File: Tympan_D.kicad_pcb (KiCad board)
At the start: 4 copper layers, 38 x 74 mm, 116 parts, among them IC1 MK66FX1M0VMD18, IC2 MKL02Z32VFG4, IC3 BC127, J1 SJ-3523-SMT-TR, J2 SJ-3524-SMT-TR-PI, J3 alt Power Pads, P1 USB_OTG, P10 CONN_01X01, P2 CONN_01X06, P3 CONN_01X06, P4 CONN_01X06, P5 CONN_01X06, P6 CONN_01X03, P7 CONN_01X01, P8 CONN_01X01, P9 CONN_01X01, SW1 CL-SB-22A, SW2 TACT_SWITCH, U1 AP2210K-3.3TRG1, U2 TLV320AIC3206IRSBT, U3 74LVC1G66, U4 LP5907MFX-1.8, U5 MCP73831, Y1 32.768kHz, Y2 16MHz

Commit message: Made Production Files
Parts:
- moved G*** 3.59 mm to (133.8, 80.5)
- moved G*** 2.10 mm to (133.8, 65.1)
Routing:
- net /IN2_R: track 28.2 -> 27.5 mm
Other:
- board text added: "1V8|M_BIAS_1 IN1_R|MCLK IN1_L|BCLK LOL|WCLK LOR|RST_1 GND|GND"
- board text added: "Alt Power 12V Max Cut V_BUS"
- board text added: "Designed in Brooklyn, NY USA Made in Taipei, Taiwan"
- board text added: "GND +V"
- board text added: "PDM_DAT|3V3 PDM_CLK|DOUT MISO_2|DIN MOSI_2|SDA2 SCK_2|SCL2 SS_2|GND"
- board text removed: "1V8/M_BIAS_1 IN1_R/MCLK IN1_L/BCLK LOL/WCLK LOR/RST_1 GND/GND"
- board text removed: "Alt Power 12V Max"
- board text removed: "Designed in Brooklyn, NY"
- board text removed: "GND BATT"
- board text removed: "TX_3/3V3 RX_3/DOUT MISO_2/DIN MOSI_2/SDA2 SCK_2/SCL2 SS_2/GND"
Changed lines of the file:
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@@
     (thickness 1.6)
     (drawings 77)
-    (tracks 1333)
+    (tracks 1335)
     (zones 0)
     (modules 116)
@@
     (36 B.SilkS user)
     (37 F.SilkS user)
-    (38 B.Mask user hide)
-    (39 F.Mask user hide)
+    (38 B.Mask user)
+    (39 F.Mask user)
     (40 Dwgs.User user hide)
     (41 Cmts.User user hide)
     (42 Eco1.User user hide)
-    (43 Eco2.User user)
+    (43 Eco2.User user hide)
     (44 Edge.Cuts user)
     (45 Margin user)
@@
   )
   (setup
-    (last_trace_width 0.2032)
+    (last_trace_width 0.25)
     (user_trace_width 0.1778)
     (user_trace_width 0.2032)
@@
     (descr BGA-144-1mm)
     (attr smd)
-    (fp_text reference IC1 (at -5.226 7.6866 180) (layer B.SilkS)
+    (fp_text reference IC1 (at -7.876 6.0866 180) (layer B.SilkS)
       (effects (font (size 1 1) (thickness 0.15)) (justify mirror))
     )
@@
     (at 132.575 100.03 180)
     (attr smd)
-    (fp_text reference Y1 (at 0.1 -1.8 180) (layer B.SilkS)
+    (fp_text reference Y1 (at 1.285 -1.67 180) (layer B.SilkS)
       (effects (font (size 0.635 0.635) (thickness 0.127)) (justify mirror))
     )
@@
     (tags "capacitor 0402")
     (attr smd)
-    (fp_text reference C34 (at 0 0.95 180) (layer B.SilkS)
+    (fp_text reference C34 (at -1.95 -0.01 180) (layer B.SilkS)
       (effects (font (size 0.635 0.635) (thickness 0.127)) (justify mirror))
     )
@@
   )
   (module Graphics:Tympan_LOGO (layer B.Cu)
-    (at 133.975 62.98 180)
+    (at 133.85 65.08 180)
     (attr smd)
     (fp_text reference G*** (at 0 0 180) (layer B.SilkS) hide
@@
   )
   (module Graphics:oshwa-logo-gear (layer B.Cu)
-    (at 131.05 78.23 180)
+    (at 133.85 80.48 180)
     (attr smd)
     (fp_text reference G*** (at 0 0 180) (layer B.SilkS) hide
@@
   (module "Tympan:alt Power Pads" (layer B.Cu)
     (at 141.9 103.68)
-    (fp_text reference J3 (at -0.5 -3) (layer B.SilkS)
+    (attr smd)
+    (fp_text reference J3 (at 3.58 1.6) (layer B.SilkS)
       (effects (font (size 0.635 0.635) (thickness 0.127)) (justify mirror))
     )
@@
   )
   (gr_circle (center 150.6 54.23) (end 153.15 54.23) (layer Cmts.User) (width 0.2))
-  (gr_text "GND     BATT" (at 145.3 99.83) (layer B.SilkS)
+  (gr_text "GND     +V" (at 145.68 100.58) (layer B.SilkS)
     (effects (font (size 1 1) (thickness 0.2)) (justify mirror))
   )
-  (gr_text "Alt Power\n12V Max" (at 145.4 97.03) (layer B.SilkS)
+  (gr_text "Alt Power\n12V Max\nCut V_BUS" (at 145.42 97.2) (layer B.SilkS)
     (effects (font (size 1 1) (thickness 0.2)) (justify mirror))
   )
@@
     (effects (font (size 1 1) (thickness 0.2)) (justify mirror))
   )
-  (gr_text "www.tympan.org\ngithub.com/tympan" (at 133.975 70.63) (layer B.SilkS)
+  (gr_text "www.tympan.org\ngithub.com/tympan" (at 133.95 73.08) (layer B.SilkS)
     (effects (font (size 1 1) (thickness 0.2)) (justify mirror))
   )
-  (gr_text "Designed in Brooklyn, NY" (at 133.975 53.305) (layer B.SilkS)
+  (gr_text "Designed in Brooklyn, NY USA\nMade in Taipei, Taiwan" (at 133.85 54.08) (layer B.SilkS)
     (effects (font (size 1 1) (thickness 0.2)) (justify mirror))
   )
@@
     (effects (font (size 0.7 0.7) (thickness 0.175)) (justify right mirror))
   )
-  (gr_text "TX_3/3V3\n\nRX_3/DOUT\n\nMISO_2/DIN\n\nMOSI_2/SDA2\n\nSCK_2/SCL2\n\nSS_2/GND\n" (at 146.3 78.13) (layer F.SilkS)
+  (gr_text "PDM_DAT|3V3\n\nPDM_CLK|DOUT\n\nMISO_2|DIN\n\nMOSI_2|SDA2\n\nSCK_2|SCL2\n\nSS_2|GND\n" (at 146.3 78.13) (layer F.SilkS)
     (effects (font (size 0.8 0.6) (thickness 0.15)) (justify right))
   )
-  (gr_text "1V8/M_BIAS_1\n\nIN1_R/MCLK\n\nIN1_L/BCLK\n\nLOL/WCLK\n\nLOR/RST_1\n\nGND/GND\n" (at 121.3 78.13) (layer F.SilkS)
+  (gr_text "1V8|M_BIAS_1\n\nIN1_R|MCLK\n\nIN1_L|BCLK\n\nLOL|WCLK\n\nLOR|RST_1\n\nGND|GND\n" (at 121.3 78.13) (layer F.SilkS)
     (effects (font (size 0.8 0.6) (thickness 0.15)) (justify left))
   )
@@
   (gr_line (start 149.85 101.23) (end 149.85 63.23) (angle 90) (layer Dwgs.User) (width 0.2))
   (gr_line (start 119.85 101.23) (end 149.85 101.23) (angle 90) (layer Dwgs.User) (width 0.2))
-  (gr_text "TYMPAN\nRevD" (at 132.45 108.58) (layer F.SilkS)
+  (gr_text "TYMPAN\nRevD" (at 132.54 107.89) (layer F.SilkS)
     (effects (font (size 1.524 1.524) (thickness 0.2)) (justify right))
   )
-  (gr_text "TYMPAN  Rev D" (at 133.75 56.28) (layer B.SilkS)
+  (gr_text "TYMPAN  Rev D" (at 133.85 58.28) (layer B.SilkS)
     (effects (font (size 1.524 1.524) (thickness 0.25)) (justify mirror))
   )
@@
     (effects (font (size 0.762 0.762) (thickness 0.1778)) (justify left mirror))
   )
-  (gr_text INPUT (at 128.075 62.03) (layer F.SilkS)
+  (gr_text INPUT (at 128.09 54.95 90) (layer F.SilkS)
     (effects (font (size 0.762 0.762) (thickness 0.1778)))
   )
-  (gr_text OUTPUT (at 139.025 61.88) (layer F.SilkS)
+  (gr_text OUTPUT (at 139.73 54.21 90) (layer F.SilkS)
     (effects (font (size 0.762 0.762) (thickness 0.1778)))
   )
@@
   (segment (start 149.801 66.38) (end 151.35 66.38) (width 0.2032) (layer B.Cu) (net 11))
   (segment (start 118.4 66.73) (end 120.15 66.73) (width 0.2032) (layer F.Cu) (net 12))
-  (segment (start 121.8 65.08) (end 136.15 65.08) (width 0.2032) (layer In2.Cu) (net 12))
-  (segment (start 120.25 66.63) (end 121.8 65.08) (width 0.2032) (layer In2.Cu) (net 12))
   (via (at 120.25 66.63) (size 0.6) (drill 0.4) (layers F.Cu B.Cu) (net 12))
   (segment (start 120.15 66.73) (end 120.25 66.63) (width 0.2032) (layer F.Cu) (net 12))
-  (via (at 136.15 65.08) (size 0.6) (drill 0.4) (layers F.Cu B.Cu) (net 12))
   (via (at 135.7 72.255) (size 0.6) (drill 0.4) (layers F.Cu B.Cu) (net 12))
   (segment (start 135.6946 72.2604) (end 135.7 72.255) (width 0.2032) (layer F.Cu) (net 12))
   (segment (start 135.6946 73.247) (end 135.6946 72.2604) (width 0.2032) (layer F.Cu) (net 12))
-  (segment (start 135.7 72.255) (end 135.025 72.255) (width 0.2032) (layer B.Cu) (net 12))
-  (segment (start 135.025 72.255) (end 134.5 71.73) (width 0.2032) (layer B.Cu) (net 12))
-  (segment (start 134.5 66.73) (end 136.15 65.08) (width 0.2032) (layer B.Cu) (net 12))
-  (segment (start 134.5 71.73) (end 134.5 66.73) (width 0.2032) (layer B.Cu) (net 12))
+  (via (at 136.48 65.790002) (size 0.6) (drill 0.4) (layers F.Cu B.Cu) (net 12))
+  (segment (start 121.089998 65.790002) (end 136.055736 65.790002) (width 0.2032) (layer In2.Cu) (net 12))
+  (segment (start 120.25 66.63) (end 121.089998 65.790002) (width 0.2032) (layer In2.Cu) (net 12))
+  (segment (start 136.055736 65.790002) (end 136.48 65.790002) (width 0.2032) (layer In2.Cu) (net 12))
+  (segment (start 135.7 72.255) (end 135.275736 72.255) (width 0.2032) (layer B.Cu) (net 12))
+  (segment (start 135.275736 72.255) (end 134.5 71.479264) (width 0.2032) (layer B.Cu) (net 12))
+  (segment (start 134.5 67.770002) (end 136.180001 66.090001) (width 0.2032) (layer B.Cu) (net 12))
+  (segment (start 134.5 71.479264) (end 134.5 67.770002) (width 0.2032) (layer B.Cu) (net 12))
+  (segment (start 136.180001 66.090001) (end 136.48 65.790002) (width 0.2032) (layer B.Cu) (net 12))
   (segment (start 116.585 67.596) (end 116.15 67.161) (width 0.2032) (layer B.Cu) (net 13))
   (segment (start 116.15 66.68) (end 117.25 66.68) (width 0.2032) (layer F.Cu) (net 13))
@@
   (segment (start 144.8 79.33) (end 144.805 79.325) (width 0.2032) (layer F.Cu) (net 199))
   (via (at 144.8 79.33) (size 0.6) (drill 0.4) (layers F.Cu B.Cu) (net 199))
-  (segment (start 148.34 74.255) (end 148.35 74.245) (width 0.2032) (layer F.Cu) (net 226))
   (segment (start 134.07514 86.68014) (end 134.07514 86.66496) (width 0.25) (layer B.Cu) (net 202))
   (segment (start 119.575 115.255) (end 122.405 115.255) (width 0.2032) (layer F.Cu) (net 204))
@@
   (segment (start 117.9 73.048) (end 117.9 85.43) (width 0.2032) (layer In1.Cu) (net 224))
   (segment (start 119.168 71.78) (end 117.9 73.048) (width 0.2032) (layer In1.Cu) (net 224))
+  (segment (start 148.34 74.255) (end 148.35 74.245) (width 0.2032) (layer F.Cu) (net 226))
   (segment (start 136.2728 76.447) (end 136.6 76.7742) (width 0.2032) (layer F.Cu) (net 226))
   (segment (start 135.6946 76.447) (end 136.2728 76.447) (width 0.2032) (layer F.Cu) (net 226))

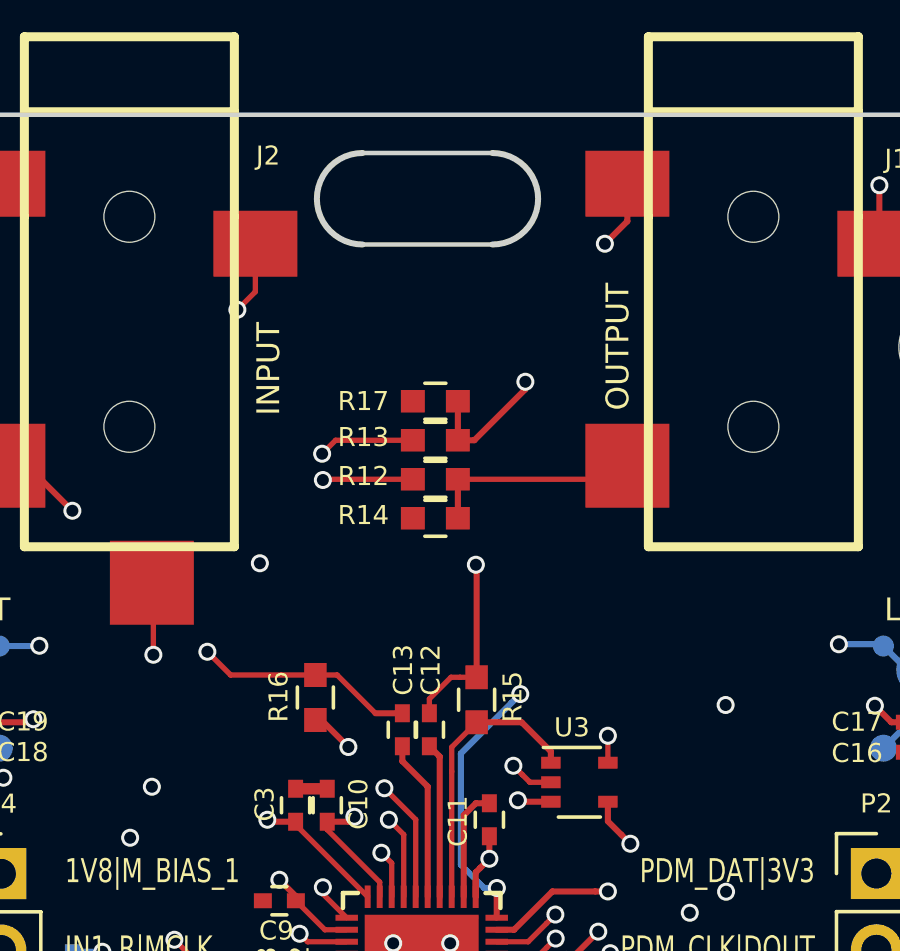
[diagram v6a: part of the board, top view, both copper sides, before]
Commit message: updated schematics
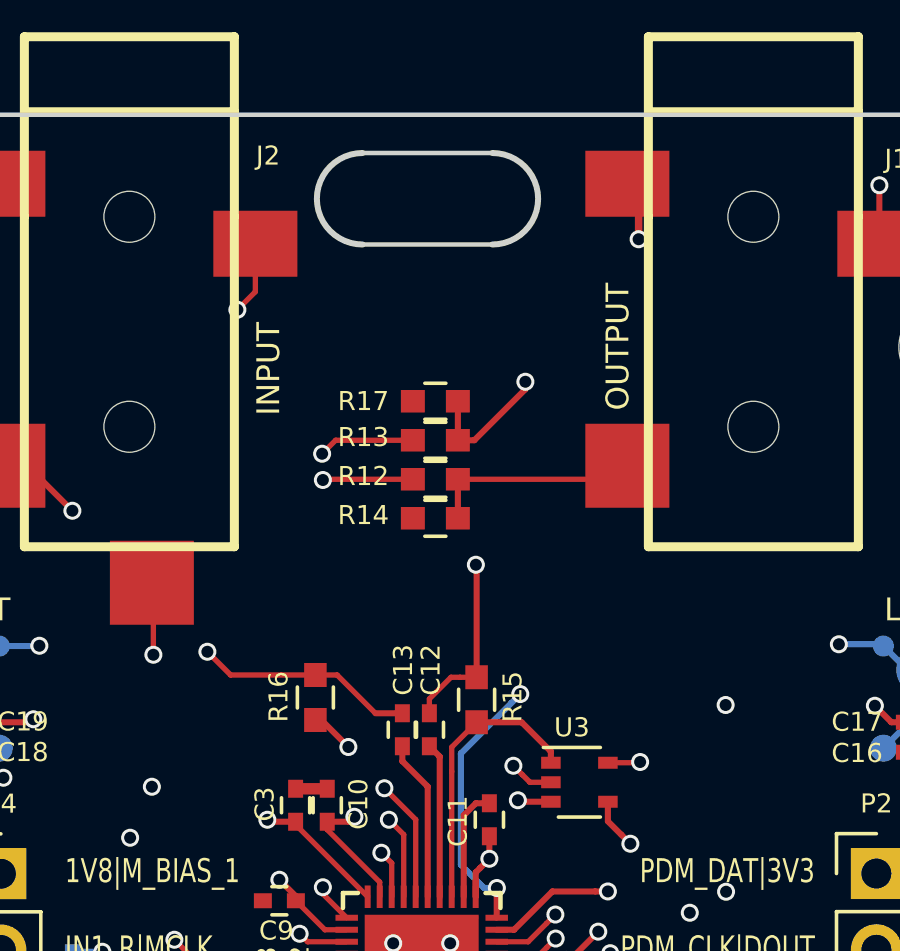
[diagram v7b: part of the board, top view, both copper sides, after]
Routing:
- net +1V8: vias 6 -> 5
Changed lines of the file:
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@@
     (thickness 1.6)
     (drawings 77)
-    (tracks 1335)
+    (tracks 1336)
     (zones 0)
     (modules 116)
@@
     (34 B.Paste user)
     (35 F.Paste user)
-    (36 B.SilkS user)
-    (37 F.SilkS user)
-    (38 B.Mask user)
-    (39 F.Mask user)
+    (36 B.SilkS user hide)
+    (37 F.SilkS user hide)
+    (38 B.Mask user hide)
+    (39 F.Mask user hide)
     (40 Dwgs.User user hide)
     (41 Cmts.User user hide)
@@
   (segment (start 135.150001 71.579991) (end 135.45 71.279992) (width 0.2032) (layer F.Cu) (net 1))
   (segment (start 135.45 71.279992) (end 135.45 70.53) (width 0.2032) (layer F.Cu) (net 1))
-  (via (at 139.3 50.78) (size 0.6) (drill 0.4) (layers F.Cu B.Cu) (net 1))
-  (segment (start 140.05 50.03) (end 140.05 48.78) (width 0.2032) (layer F.Cu) (net 1))
-  (segment (start 139.3 50.78) (end 140.05 50.03) (width 0.2032) (layer F.Cu) (net 1))
-  (segment (start 138.6 51.48) (end 139.3 50.78) (width 0.2032) (layer In1.Cu) (net 1))
-  (segment (start 138.6 70.23) (end 138.6 51.48) (width 0.2032) (layer In1.Cu) (net 1))
-  (segment (start 138.2 70.63) (end 138.6 70.23) (width 0.2032) (layer In1.Cu) (net 1))
-  (segment (start 132.3 70.63) (end 138.2 70.63) (width 0.2032) (layer In1.Cu) (net 1))
-  (segment (start 131.85 71.08) (end 132.3 70.63) (width 0.2032) (layer In1.Cu) (net 1))
   (via (at 126.95 102.429996) (size 0.6) (drill 0.4) (layers F.Cu B.Cu) (net 1))
   (segment (start 126.95 101.305) (end 126.95 102.429996) (width 0.2032) (layer B.Cu) (net 1))
@@
   (segment (start 138.67 79.53) (end 137.94 80.26) (width 0.381) (layer F.Cu) (net 1))
   (segment (start 138.85 79.53) (end 138.67 79.53) (width 0.381) (layer F.Cu) (net 1))
+  (segment (start 139.725 69.105) (end 139.725 51.205) (width 0.2032) (layer In1.Cu) (net 1))
+  (segment (start 132.3 70.63) (end 138.2 70.63) (width 0.2032) (layer In1.Cu) (net 1))
+  (segment (start 131.85 71.08) (end 132.3 70.63) (width 0.2032) (layer In1.Cu) (net 1))
+  (segment (start 138.2 70.63) (end 139.725 69.105) (width 0.2032) (layer In1.Cu) (net 1))
+  (via (at 140.425 50.63) (size 0.6) (drill 0.4) (layers F.Cu B.Cu) (net 1))
+  (segment (start 140.3 50.63) (end 140.425 50.63) (width 0.25) (layer In1.Cu) (net 1))
+  (segment (start 139.725 51.205) (end 140.3 50.63) (width 0.25) (layer In1.Cu) (net 1))
+  (segment (start 140.425 49.155) (end 140.05 48.78) (width 0.25) (layer F.Cu) (net 1))
+  (segment (start 140.425 50.63) (end 140.425 49.155) (width 0.25) (layer F.Cu) (net 1))
   (segment (start 134.65 111.58) (end 133.05 111.58) (width 0.2032) (layer F.Cu) (net 2))
   (via (at 133.05 111.58) (size 0.6) (drill 0.4) (layers F.Cu B.Cu) (net 2))
@@
   (segment (start 134.9946 77.547) (end 134.9946 77.8083) (width 0.1778) (layer F.Cu) (net 2))
   (segment (start 134.9946 77.547) (end 134.9946 77.694) (width 0.1778) (layer F.Cu) (net 2))
-  (via (at 139.4 67.180002) (size 0.6) (drill 0.4) (layers F.Cu B.Cu) (net 2))
-  (segment (start 139.4 68.08) (end 139.4 67.180002) (width 0.1778) (layer F.Cu) (net 2))
   (segment (start 128.9238 69.98) (end 128.9909 70.0471) (width 0.1778) (layer F.Cu) (net 2))
   (segment (start 131.3946 72.547) (end 128.9909 70.1433) (width 0.1778) (layer F.Cu) (net 2))
@@
   (segment (start 137.367699 78.4393) (end 137.99 79.061601) (width 0.381) (layer F.Cu) (net 2))
   (segment (start 137.2006 78.4393) (end 137.367699 78.4393) (width 0.381) (layer F.Cu) (net 2))
+  (via (at 140.475 68.055) (size 0.6) (drill 0.4) (layers F.Cu B.Cu) (net 2))
+  (segment (start 139.4 68.08) (end 140.45 68.08) (width 0.1778) (layer F.Cu) (net 2))
+  (segment (start 140.45 68.08) (end 140.475 68.055) (width 0.1778) (layer F.Cu) (net 2))
   (segment (start 130.6946 75.247) (end 130.1879 75.247) (width 0.1778) (layer F.Cu) (net 3))
   (segment (start 129.5155 75.9194) (end 129.1179 75.9194) (width 0.1778) (layer F.Cu) (net 3))
@@
   (segment (start 117.6 106.63) (end 118.65 107.68) (width 0.2032) (layer F.Cu) (net 5))
   (segment (start 117.6 102.84) (end 117.6 106.63) (width 0.2032) (layer F.Cu) (net 5))
-  (via (at 127.8 61.43) (size 0.6) (drill 0.4) (layers F.Cu B.Cu) (net 6))
   (segment (start 147.1 88.63) (end 148.5 88.63) (width 0.381) (layer B.Cu) (net 6))
   (via (at 148.5 88.63) (size 0.6) (drill 0.4) (layers F.Cu B.Cu) (net 6))

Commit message: added some more dimensions
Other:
- board text added: "OD 3mm x4"
- board text added: "r=1mm x4"
- board text removed: "OD 3mm"
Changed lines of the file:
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@@
   (general
     (thickness 1.6)
-    (drawings 77)
+    (drawings 83)
     (tracks 1336)
     (zones 0)
@@
     (34 B.Paste user)
     (35 F.Paste user)
-    (36 B.SilkS user hide)
-    (37 F.SilkS user hide)
-    (38 B.Mask user hide)
-    (39 F.Mask user hide)
-    (40 Dwgs.User user hide)
+    (36 B.SilkS user)
+    (37 F.SilkS user)
+    (38 B.Mask user)
+    (39 F.Mask user)
+    (40 Dwgs.User user)
     (41 Cmts.User user hide)
     (42 Eco1.User user hide)
-    (43 Eco2.User user hide)
+    (43 Eco2.User user)
     (44 Edge.Cuts user)
     (45 Margin user)
@@
     )
   )
+  (gr_line (start 113.925 52.93) (end 113.6 51.905) (layer Dwgs.User) (width 0.2))
+  (gr_line (start 106.725 50.78) (end 113.925 52.93) (layer Dwgs.User) (width 0.2))
+  (gr_line (start 114.025 45.03) (end 114 45.055) (layer Dwgs.User) (width 0.2))
+  (gr_line (start 114.025 45.805) (end 114.025 45.03) (layer Dwgs.User) (width 0.2))
+  (gr_line (start 110.85 43.505) (end 114.025 45.805) (layer Dwgs.User) (width 0.2))
+  (gr_text "r=1mm x4" (at 108.625 42.68) (layer Dwgs.User)
+    (effects (font (size 1 1) (thickness 0.2)))
+  )
   (gr_text "Cut trace btw\nVPP | V_BAT\nto attach your\nown RTC battery\nto V_BAT | GND" (at 120.55 112.78) (layer B.SilkS)
     (effects (font (size 0.6 0.8) (thickness 0.15)) (justify mirror))
   )
-  (gr_text "OD 3mm" (at 112.79 50.43 90) (layer Dwgs.User)
+  (gr_text "OD 3mm x4" (at 104.475 49.505) (layer Dwgs.User)
     (effects (font (size 1 1) (thickness 0.2)))
   )
@@
   (gr_line (start 117.25 95.58) (end 122.35 95.58) (angle 90) (layer Eco2.User) (width 0.2))
   (gr_circle (center 117.25 91.555) (end 121.65 91.555) (layer Eco2.User) (width 0.2))
-  (gr_line (start 114.85 46.48) (end 114.85 109.48) (angle 90) (layer Dwgs.User) (width 0.2))
-  (gr_line (start 152.85 46.48) (end 114.85 46.48) (angle 90) (layer Dwgs.User) (width 0.2))
-  (gr_line (start 152.85 109.48) (end 152.85 46.48) (angle 90) (layer Dwgs.User) (width 0.2))
-  (gr_line (start 114.85 109.48) (end 152.85 109.48) (angle 90) (layer Dwgs.User) (width 0.2))
+  (gr_line (start 114.85 46.48) (end 114.85 109.48) (angle 90) (layer Eco1.User) (width 0.2))
+  (gr_line (start 152.85 46.48) (end 114.85 46.48) (angle 90) (layer Eco1.User) (width 0.2))
+  (gr_line (start 152.85 109.48) (end 152.85 46.48) (angle 90) (layer Eco1.User) (width 0.2))
+  (gr_line (start 114.85 109.48) (end 152.85 109.48) (angle 90) (layer Eco1.User) (width 0.2))
   (gr_line (start 119.95 95.705) (end 119.95 87.705) (angle 90) (layer Cmts.User) (width 0.2))
   (gr_line (start 116.2 87.705) (end 116.2 95.705) (angle 90) (layer Cmts.User) (width 0.2))
@@
   (gr_line (start 152.85 120.48) (end 152.85 46.48) (angle 90) (layer Eco1.User) (width 0.2))
   (gr_line (start 114.85 120.48) (end 152.85 120.48) (angle 90) (layer Eco1.User) (width 0.2))
-  (gr_line (start 119.85 63.23) (end 119.85 101.23) (angle 90) (layer Dwgs.User) (width 0.2))
-  (gr_line (start 149.85 63.23) (end 119.85 63.23) (angle 90) (layer Dwgs.User) (width 0.2))
-  (gr_line (start 149.85 101.23) (end 149.85 63.23) (angle 90) (layer Dwgs.User) (width 0.2))
-  (gr_line (start 119.85 101.23) (end 149.85 101.23) (angle 90) (layer Dwgs.User) (width 0.2))
+  (gr_line (start 119.85 63.23) (end 119.85 101.23) (angle 90) (layer Eco1.User) (width 0.2))
+  (gr_line (start 149.85 63.23) (end 119.85 63.23) (angle 90) (layer Eco1.User) (width 0.2))
+  (gr_line (start 149.85 101.23) (end 149.85 63.23) (angle 90) (layer Eco1.User) (width 0.2))
+  (gr_line (start 119.85 101.23) (end 149.85 101.23) (angle 90) (layer Eco1.User) (width 0.2))
   (gr_text "TYMPAN\nRevD" (at 132.54 107.89) (layer F.SilkS)
     (effects (font (size 1.524 1.524) (thickness 0.2)) (justify right))
